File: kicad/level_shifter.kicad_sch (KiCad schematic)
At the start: 30 parts, among them U3 74LVC2T45GT, U4 74LVC2T45GT, U5 74LVC2T45GT, U6 74LVC2T45GT

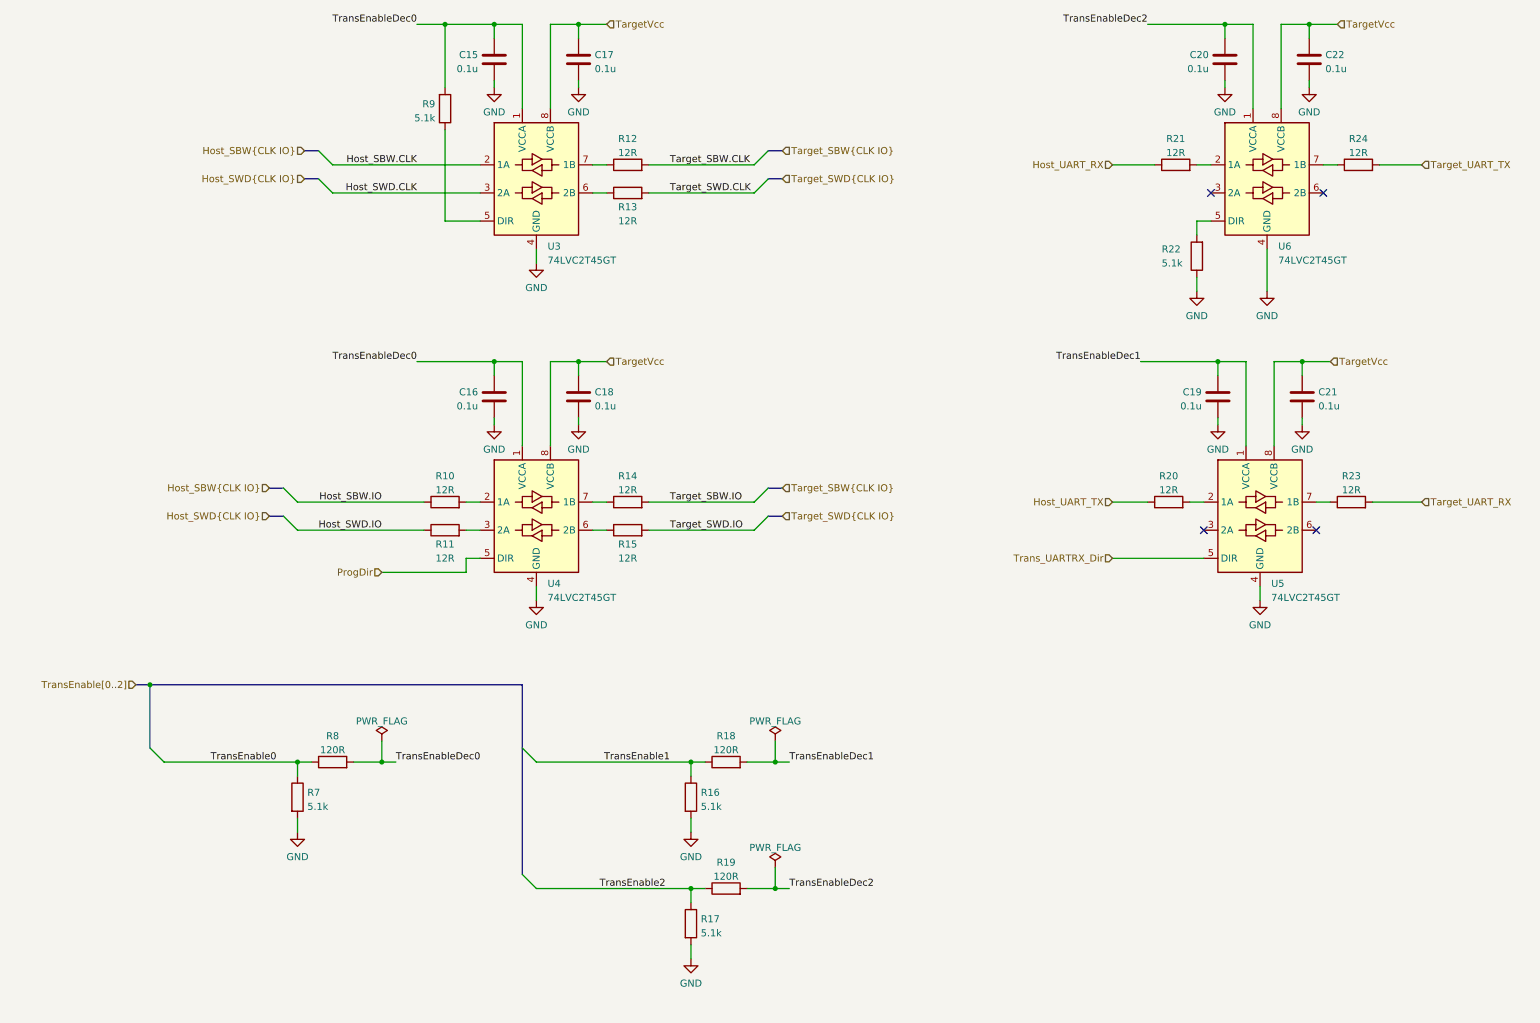
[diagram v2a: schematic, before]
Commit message: replace target supply diode with analog switch
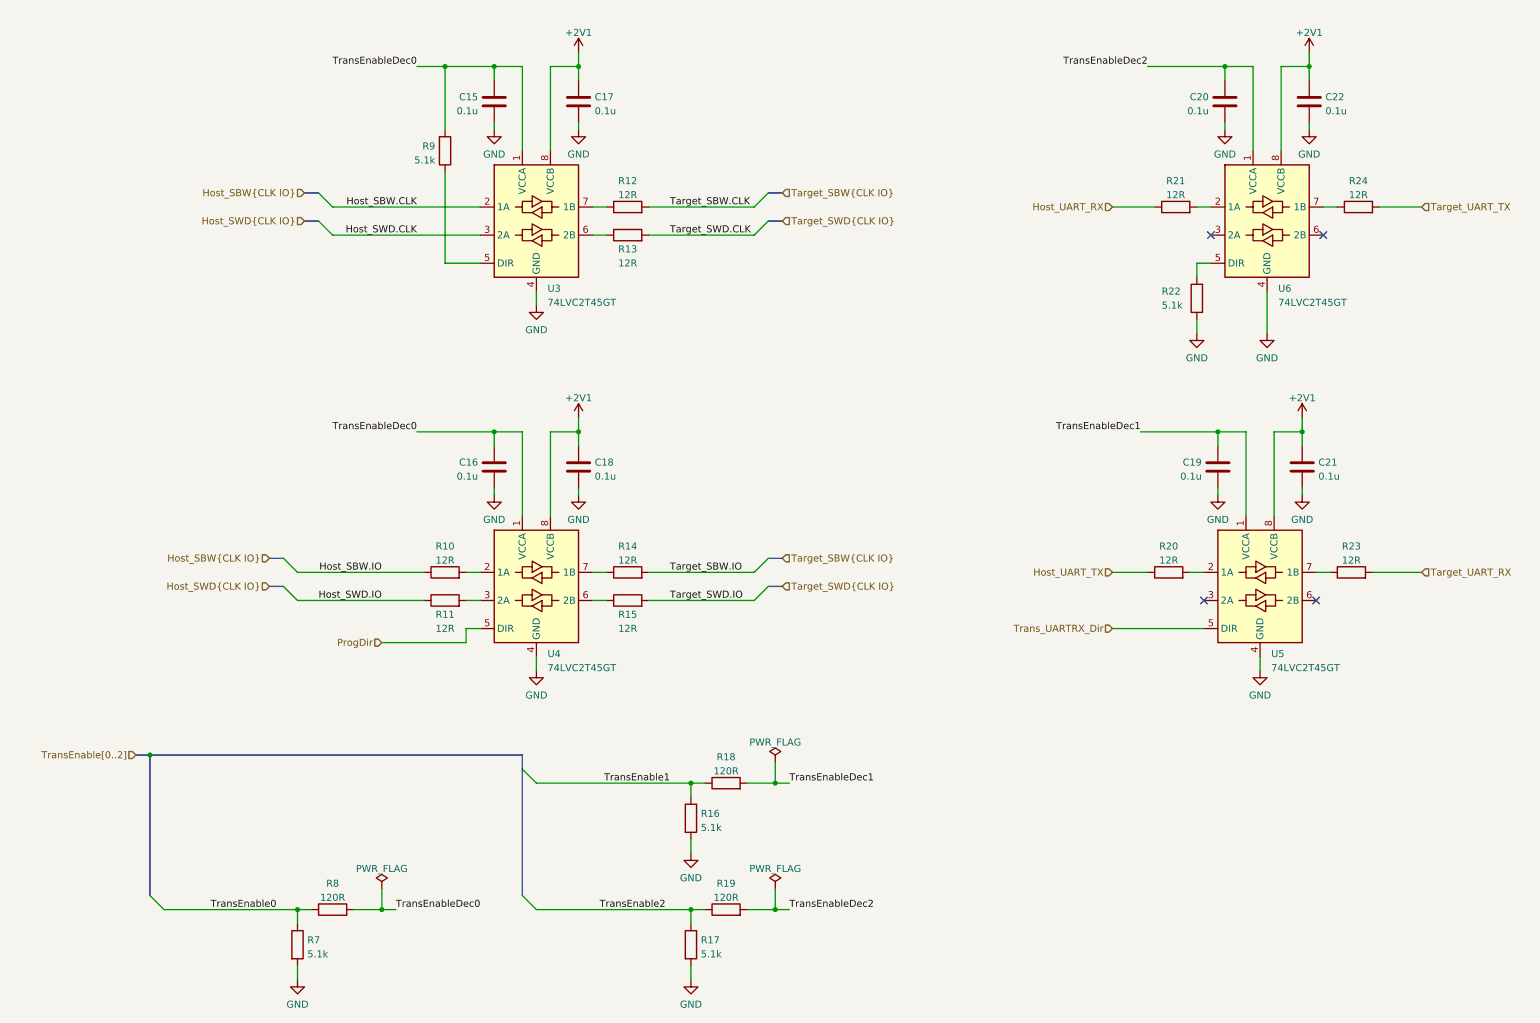
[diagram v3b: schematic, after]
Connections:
- net TargetVcc renamed +2V1
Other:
- moved on the sheet: C15, C16, C17, C18, C19, C20, C21, C22, R10, R11, R12, R13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

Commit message: add MPNs in schematics
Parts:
- C15, C16, C17, C18, C19, C20, C21, C22: MPN (none) -> CL05A104KA5NNNC
- R10, R11, R12, R13, R14, R15, R20, R21, R23, R24: MPN (none) -> RMCF0402FT12R0
- R16, R17, R22, R7, R9: MPN (none) -> CR0402-FX-5101GLF
- R18, R19, R8: MPN (none) -> CR0402-FX-1200GLF
- U3, U4, U5, U6: MPN (none) -> 74LVC2T45GT,115
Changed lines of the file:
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@@
+      (effects (font (size 1.27 1.27)) hide)
+    )
+    (property "MPN" "74LVC2T45GT,115" (id 4) (at 236.22 119.38 0)
       (effects (font (size 1.27 1.27)) hide)
     )
@@
       (effects (font (size 1.27 1.27)) hide)
     )
+    (property "MPN" "74LVC2T45GT,115" (id 4) (at 105.41 53.34 0)
+      (effects (font (size 1.27 1.27)) hide)
+    )
     (pin "1")
     (pin "2")
@@
       (effects (font (size 1.27 1.27)) hide)
     )
+    (property "MPN" "RMCF0402FT12R0" (id 4) (at 220.98 50.8 0)
+      (effects (font (size 1.27 1.27)) hide)
+    )
     (pin "1")
     (pin "2")
@@
     )
     (property "Datasheet" "~" (id 3) (at 62.23 184.15 0)
+      (effects (font (size 1.27 1.27)) hide)
+    )
+    (property "MPN" "CR0402-FX-5101GLF" (id 4) (at 62.23 184.15 0)
       (effects (font (size 1.27 1.27)) hide)
     )
@@
       (effects (font (size 1.27 1.27)) hide)
     )
+    (property "MPN" "CR0402-FX-5101GLF" (id 4) (at 133.35 161.29 0)
+      (effects (font (size 1.27 1.27)) hide)
+    )
     (pin "1")
     (pin "2")
@@
     )
     (property "Datasheet" "~" (id 3) (at 245.11 31.75 0)
+      (effects (font (size 1.27 1.27)) hide)
+    )
+    (property "MPN" "CL05A104KA5NNNC" (id 4) (at 245.11 31.75 0)
       (effects (font (size 1.27 1.27)) hide)
     )
@@
       (effects (font (size 1.27 1.27)) hide)
     )
+    (property "MPN" "RMCF0402FT12R0" (id 4) (at 252.73 116.84 0)
+      (effects (font (size 1.27 1.27)) hide)
+    )
     (pin "1")
     (pin "2")
@@
     )
     (property "Datasheet" "~" (id 3) (at 113.03 31.75 0)
+      (effects (font (size 1.27 1.27)) hide)
+    )
+    (property "MPN" "CL05A104KA5NNNC" (id 4) (at 113.03 31.75 0)
       (effects (font (size 1.27 1.27)) hide)
     )
@@
       (effects (font (size 1.27 1.27)) hide)
     )
+    (property "MPN" "CR0402-FX-1200GLF" (id 4) (at 139.7 177.8 0)
+      (effects (font (size 1.27 1.27)) hide)
+    )
     (pin "1")
     (pin "2")
@@
     )
     (property "Datasheet" "~" (id 3) (at 243.84 97.79 0)
+      (effects (font (size 1.27 1.27)) hide)
+    )
+    (property "MPN" "CL05A104KA5NNNC" (id 4) (at 243.84 97.79 0)
       (effects (font (size 1.27 1.27)) hide)
     )
@@
     )
     (property "Datasheet" "~" (id 3) (at 228.6 97.79 0)
+      (effects (font (size 1.27 1.27)) hide)
+    )
+    (property "MPN" "CL05A104KA5NNNC" (id 4) (at 228.6 97.79 0)
       (effects (font (size 1.27 1.27)) hide)
     )
@@
     )
     (property "Datasheet" "~" (id 3) (at 139.7 154.94 0)
+      (effects (font (size 1.27 1.27)) hide)
+    )
+    (property "MPN" "CR0402-FX-1200GLF" (id 4) (at 139.7 154.94 0)
       (effects (font (size 1.27 1.27)) hide)
     )
@@
       (effects (font (size 1.27 1.27)) hide)
     )
+    (property "MPN" "RMCF0402FT12R0" (id 4) (at 121.92 55.88 0)
+      (effects (font (size 1.27 1.27)) hide)
+    )
     (pin "1")
     (pin "2")
@@
     )
     (property "Datasheet" "~" (id 3) (at 97.79 97.79 0)
+      (effects (font (size 1.27 1.27)) hide)
+    )
+    (property "MPN" "CL05A104KA5NNNC" (id 4) (at 97.79 97.79 0)
       (effects (font (size 1.27 1.27)) hide)
     )
@@
       (effects (font (size 1.27 1.27)) hide)
     )
+    (property "MPN" "CR0402-FX-1200GLF" (id 4) (at 68.58 177.8 0)
+      (effects (font (size 1.27 1.27)) hide)
+    )
     (pin "1")
     (pin "2")
@@
     )
     (property "Datasheet" "~" (id 3) (at 88.9 40.64 0)
+      (effects (font (size 1.27 1.27)) hide)
+    )
+    (property "MPN" "CR0402-FX-5101GLF" (id 4) (at 88.9 40.64 0)
       (effects (font (size 1.27 1.27)) hide)
     )
@@
       (effects (font (size 1.27 1.27)) hide)
     )
+    (property "MPN" "RMCF0402FT12R0" (id 4) (at 88.9 121.92 0)
+      (effects (font (size 1.27 1.27)) hide)
+    )
     (pin "1")
     (pin "2")
@@
     )
     (property "Datasheet" "~" (id 3) (at 113.03 97.79 0)
+      (effects (font (size 1.27 1.27)) hide)
+    )
+    (property "MPN" "CL05A104KA5NNNC" (id 4) (at 113.03 97.79 0)
       (effects (font (size 1.27 1.27)) hide)
     )
@@
       (effects (font (size 1.27 1.27)) hide)
     )
+    (property "MPN" "RMCF0402FT12R0" (id 4) (at 88.9 116.84 0)
+      (effects (font (size 1.27 1.27)) hide)
+    )
     (pin "1")
     (pin "2")
@@
       (effects (font (size 1.27 1.27)) hide)
     )
+    (property "MPN" "RMCF0402FT12R0" (id 4) (at 121.92 50.8 0)
+      (effects (font (size 1.27 1.27)) hide)
+    )
     (pin "1")
     (pin "2")
@@
     )
     (property "Datasheet" "https://assets.nexperia.com/documents/data-sheet/74LVC_LVCH2T45.pdf" (id 3) (at 238.76 78.74 0)
+      (effects (font (size 1.27 1.27)) hide)
+    )
+    (property "MPN" "74LVC2T45GT,115" (id 4) (at 237.49 53.34 0)
       (effects (font (size 1.27 1.27)) hide)
     )
@@
       (effects (font (size 1.27 1.27)) hide)
     )
+    (property "MPN" "RMCF0402FT12R0" (id 4) (at 121.92 116.84 0)
+      (effects (font (size 1.27 1.27)) hide)
+    )
     (pin "1")
     (pin "2")
@@
     )
     (property "Datasheet" "~" (id 3) (at 224.79 67.31 0)
+      (effects (font (size 1.27 1.27)) hide)
+    )
+    (property "MPN" "CR0402-FX-5101GLF" (id 4) (at 224.79 67.31 0)
       (effects (font (size 1.27 1.27)) hide)
     )
@@
       (effects (font (size 1.27 1.27)) hide)
     )
+    (property "MPN" "RMCF0402FT12R0" (id 4) (at 121.92 121.92 0)
+      (effects (font (size 1.27 1.27)) hide)
+    )
     (pin "1")
     (pin "2")
@@
     )
     (property "Datasheet" "~" (id 3) (at 97.79 31.75 0)
+      (effects (font (size 1.27 1.27)) hide)
+    )
+    (property "MPN" "CL05A104KA5NNNC" (id 4) (at 97.79 31.75 0)
       (effects (font (size 1.27 1.27)) hide)
     )
@@
       (effects (font (size 1.27 1.27)) hide)
     )
+    (property "MPN" "RMCF0402FT12R0" (id 4) (at 219.71 116.84 0)
+      (effects (font (size 1.27 1.27)) hide)
+    )
     (pin "1")
     (pin "2")
@@
     )
     (property "Datasheet" "https://assets.nexperia.com/documents/data-sheet/74LVC_LVCH2T45.pdf" (id 3) (at 106.68 144.78 0)
+      (effects (font (size 1.27 1.27)) hide)
+    )
+    (property "MPN" "74LVC2T45GT,115" (id 4) (at 105.41 119.38 0)
       (effects (font (size 1.27 1.27)) hide)
     )
@@
       (effects (font (size 1.27 1.27)) hide)
     )
+    (property "MPN" "RMCF0402FT12R0" (id 4) (at 254 50.8 0)
+      (effects (font (size 1.27 1.27)) hide)
+    )
     (pin "1")
     (pin "2")
@@
     )
     (property "Datasheet" "~" (id 3) (at 229.87 31.75 0)
+      (effects (font (size 1.27 1.27)) hide)
+    )
+    (property "MPN" "CL05A104KA5NNNC" (id 4) (at 229.87 31.75 0)
       (effects (font (size 1.27 1.27)) hide)
     )
@@
       (effects (font (size 1.27 1.27)) hide)
     )
+    (property "MPN" "CR0402-FX-5101GLF" (id 4) (at 133.35 184.15 0)
+      (effects (font (size 1.27 1.27)) hide)
+    )
